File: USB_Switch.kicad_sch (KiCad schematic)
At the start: 2 parts, among them J1 Conn_01x06, J4 Conn_01x08

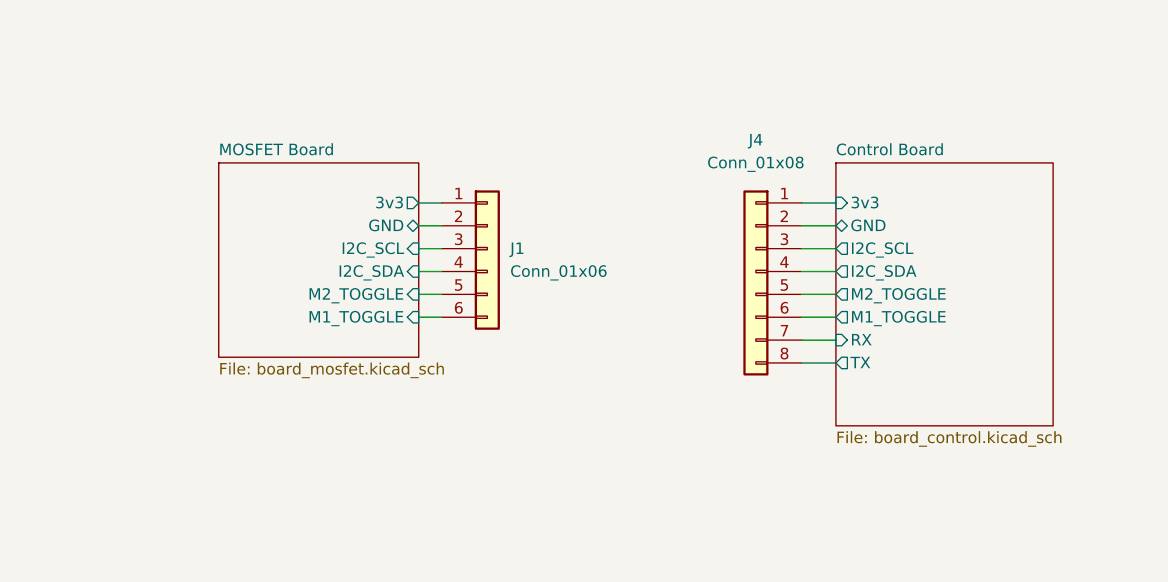
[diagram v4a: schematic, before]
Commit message: Made schematics pretty, added photos, added README
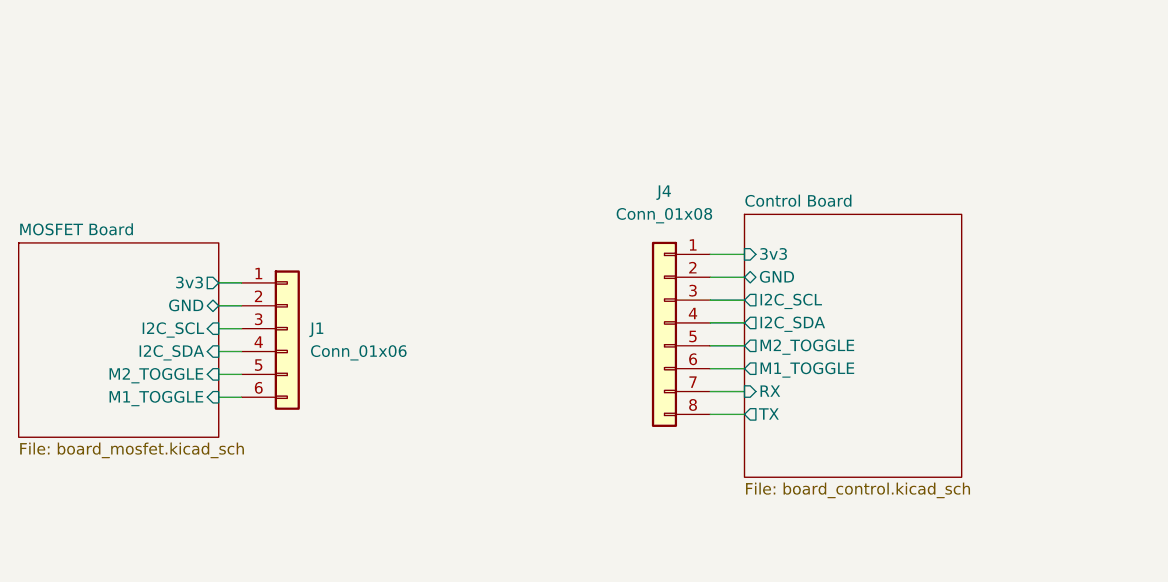
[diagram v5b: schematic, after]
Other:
- title: Smart USB Port -> Wifi USB Port
- moved on the sheet: J1, J4
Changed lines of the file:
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@@
 (kicad_sch (version 20211123) (generator eeschema)
-  (paper "A4")
+  (paper "A5")
   (title_block
-    (title "Smart USB Port")
-    (date "2022-10-23")
-    (rev "0.1")
+    (title "Wifi USB Port")
+    (date "2023-02-05")
+    (rev "0.2.0")
   )
-  (wire (pts (xy 137.795 48.895) (xy 141.605 48.895))
+  (wire (pts (xy 127.635 54.61) (xy 131.445 54.61))
     (stroke (width 0) (type default) (color 0 0 0 0))
   )
-  (wire (pts (xy 137.795 51.435) (xy 141.605 51.435))
+  (wire (pts (xy 127.635 57.15) (xy 131.445 57.15))
     (stroke (width 0) (type default) (color 0 0 0 0))
   )
-  (wire (pts (xy 137.795 59.055) (xy 141.605 59.055))
+  (wire (pts (xy 127.635 64.77) (xy 131.445 64.77))
     (stroke (width 0) (type default) (color 0 0 0 0))
   )
-  (wire (pts (xy 137.795 53.975) (xy 141.605 53.975))
+  (wire (pts (xy 127.635 59.69) (xy 131.445 59.69))
     (stroke (width 0) (type default) (color 0 0 0 0))
   )
-  (wire (pts (xy 97.79 61.595) (xy 95.25 61.595))
+  (wire (pts (xy 75.565 70.485) (xy 73.025 70.485))
     (stroke (width 0) (type default) (color 0 0 0 0))
   )
-  (wire (pts (xy 137.795 64.135) (xy 141.605 64.135))
+  (wire (pts (xy 127.635 69.85) (xy 131.445 69.85))
     (stroke (width 0) (type default) (color 0 0 0 0))
   )
-  (wire (pts (xy 97.79 59.055) (xy 95.25 59.055))
+  (wire (pts (xy 75.565 67.945) (xy 73.025 67.945))
     (stroke (width 0) (type default) (color 0 0 0 0))
   )
-  (wire (pts (xy 97.79 56.515) (xy 95.25 56.515))
+  (wire (pts (xy 75.565 65.405) (xy 73.025 65.405))
     (stroke (width 0) (type default) (color 0 0 0 0))
   )
-  (wire (pts (xy 137.795 61.595) (xy 141.605 61.595))
+  (wire (pts (xy 127.635 67.31) (xy 131.445 67.31))
     (stroke (width 0) (type default) (color 0 0 0 0))
   )
-  (wire (pts (xy 97.79 51.435) (xy 95.25 51.435))
+  (wire (pts (xy 75.565 60.325) (xy 73.025 60.325))
     (stroke (width 0) (type default) (color 0 0 0 0))
   )
-  (wire (pts (xy 97.79 48.895) (xy 95.25 48.895))
+  (wire (pts (xy 75.565 57.785) (xy 73.025 57.785))
     (stroke (width 0) (type default) (color 0 0 0 0))
   )
-  (wire (pts (xy 97.79 53.975) (xy 95.25 53.975))
+  (wire (pts (xy 75.565 62.865) (xy 73.025 62.865))
     (stroke (width 0) (type default) (color 0 0 0 0))
   )
-  (wire (pts (xy 137.795 66.675) (xy 141.605 66.675))
+  (wire (pts (xy 127.635 72.39) (xy 131.445 72.39))
     (stroke (width 0) (type default) (color 0 0 0 0))
   )
-  (wire (pts (xy 137.795 56.515) (xy 141.605 56.515))
+  (wire (pts (xy 127.635 62.23) (xy 131.445 62.23))
     (stroke (width 0) (type default) (color 0 0 0 0))
   )
-  (symbol (lib_id "Connector_Generic:Conn_01x08") (at 132.715 56.515 0) (mirror y) (unit 1)
+  (symbol (lib_id "Connector_Generic:Conn_01x08") (at 122.555 62.23 0) (mirror y) (unit 1)
     (in_bom yes) (on_board yes) (fields_autoplaced)
-    (property "Reference" "J4" (id 0) (at 132.715 41.91 0))
-    (property "Value" "Conn_01x08" (id 1) (at 132.715 44.45 0))
-    (property "Footprint" "Connector_PinHeader_2.54mm:PinHeader_1x08_P2.54mm_Vertical" (id 2) (at 132.715 56.515 0)
+    (property "Reference" "J4" (id 0) (at 122.555 47.625 0))
+    (property "Value" "Conn_01x08" (id 1) (at 122.555 50.165 0))
+    (property "Footprint" "Connector_PinHeader_2.54mm:PinHeader_1x08_P2.54mm_Vertical" (id 2) (at 122.555 62.23 0)
       (effects (font (size 1.27 1.27)) hide)
     )
-    (property "Datasheet" "~" (id 3) (at 132.715 56.515 0)
+    (property "Datasheet" "~" (id 3) (at 122.555 62.23 0)
       (effects (font (size 1.27 1.27)) hide)
     )
@@
     (pin "8")
   )
-  (symbol (lib_id "Connector_Generic:Conn_01x06") (at 102.87 53.975 0) (unit 1)
+  (symbol (lib_id "Connector_Generic:Conn_01x06") (at 80.645 62.865 0) (unit 1)
     (in_bom yes) (on_board yes) (fields_autoplaced)
-    (property "Reference" "J1" (id 0) (at 105.41 53.9749 0)
+    (property "Reference" "J1" (id 0) (at 83.185 62.8649 0)
       (effects (font (size 1.27 1.27)) (justify left))
     )
-    (property "Value" "Conn_01x06" (id 1) (at 105.41 56.5149 0)
+    (property "Value" "Conn_01x06" (id 1) (at 83.185 65.4049 0)
       (effects (font (size 1.27 1.27)) (justify left))
     )
-    (property "Footprint" "Connector_PinHeader_2.54mm:PinHeader_1x06_P2.54mm_Vertical" (id 2) (at 102.87 53.975 0)
+    (property "Footprint" "Connector_PinHeader_2.54mm:PinHeader_1x06_P2.54mm_Vertical" (id 2) (at 80.645 62.865 0)
       (effects (font (size 1.27 1.27)) hide)
     )
-    (property "Datasheet" "~" (id 3) (at 102.87 53.975 0)
+    (property "Datasheet" "~" (id 3) (at 80.645 62.865 0)
       (effects (font (size 1.27 1.27)) hide)
     )
-    (property "LCSC Part Number" "" (id 4) (at 102.87 53.975 0)
+    (property "LCSC Part Number" "" (id 4) (at 80.645 62.865 0)
       (effects (font (size 1.27 1.27)) hide)
     )
-    (property "Manufacturer" "" (id 5) (at 102.87 53.975 0)
+    (property "Manufacturer" "" (id 5) (at 80.645 62.865 0)
       (effects (font (size 1.27 1.27)) hide)
     )
-    (property "Manufacturer Part Number" "" (id 6) (at 102.87 53.975 0)
+    (property "Manufacturer Part Number" "" (id 6) (at 80.645 62.865 0)
       (effects (font (size 1.27 1.27)) hide)
     )
@@
     (pin "6")
   )
-  (sheet (at 141.605 44.45) (size 24.13 29.21) (fields_autoplaced)
+  (sheet (at 131.445 50.165) (size 24.13 29.21) (fields_autoplaced)
     (stroke (width 0.1524) (type solid) (color 0 0 0 0))
     (fill (color 0 0 0 0.0000))
-    (property "Sheet name" "Control Board" (id 0) (at 141.605 43.7384 0)
+    (property "Sheet name" "Control Board" (id 0) (at 131.445 49.4534 0)
       (effects (font (size 1.27 1.27)) (justify left bottom))
     )
-    (property "Sheet file" "board_control.kicad_sch" (id 1) (at 141.605 74.2446 0)
+    (property "Sheet file" "board_control.kicad_sch" (id 1) (at 131.445 79.9596 0)
       (effects (font (size 1.27 1.27)) (justify left top))
     )
-    (pin "3v3" input (at 141.605 48.895 180)
+    (pin "3v3" input (at 131.445 54.61 180)
       (effects (font (size 1.27 1.27)) (justify left))
     )
-    (pin "GND" bidirectional (at 141.605 51.435 180)
+    (pin "GND" bidirectional (at 131.445 57.15 180)
       (effects (font (size 1.27 1.27)) (justify left))
     )
-    (pin "I2C_SCL" output (at 141.605 53.975 180)
+    (pin "I2C_SCL" output (at 131.445 59.69 180)
       (effects (font (size 1.27 1.27)) (justify left))
     )
-    (pin "I2C_SDA" output (at 141.605 56.515 180)
+    (pin "I2C_SDA" output (at 131.445 62.23 180)
       (effects (font (size 1.27 1.27)) (justify left))
     )
-    (pin "M2_TOGGLE" output (at 141.605 59.055 180)
+    (pin "M2_TOGGLE" output (at 131.445 64.77 180)
       (effects (font (size 1.27 1.27)) (justify left))
     )
-    (pin "M1_TOGGLE" output (at 141.605 61.595 180)
+    (pin "M1_TOGGLE" output (at 131.445 67.31 180)
       (effects (font (size 1.27 1.27)) (justify left))
     )
-    (pin "TX" output (at 141.605 66.675 180)
+    (pin "TX" output (at 131.445 72.39 180)
       (effects (font (size 1.27 1.27)) (justify left))
     )
-    (pin "RX" input (at 141.605 64.135 180)
+    (pin "RX" input (at 131.445 69.85 180)
       (effects (font (size 1.27 1.27)) (justify left))
     )
   )
-  (sheet (at 73.025 44.45) (size 22.225 21.59) (fields_autoplaced)
+  (sheet (at 50.8 53.34) (size 22.225 21.59) (fields_autoplaced)
     (stroke (width 0.1524) (type solid) (color 0 0 0 0))
     (fill (color 0 0 0 0.0000))
-    (property "Sheet name" "MOSFET Board" (id 0) (at 73.025 43.7384 0)
+    (property "Sheet name" "MOSFET Board" (id 0) (at 50.8 52.6284 0)
       (effects (font (size 1.27 1.27)) (justify left bottom))
     )
-    (property "Sheet file" "board_mosfet.kicad_sch" (id 1) (at 73.025 66.6246 0)
+    (property "Sheet file" "board_mosfet.kicad_sch" (id 1) (at 50.8 75.5146 0)
       (effects (font (size 1.27 1.27)) (justify left top))
     )
-    (pin "3v3" output (at 95.25 48.895 0)
+    (pin "3v3" output (at 73.025 57.785 0)
       (effects (font (size 1.27 1.27)) (justify right))
     )
-    (pin "GND" bidirectional (at 95.25 51.435 0)
+    (pin "GND" bidirectional (at 73.025 60.325 0)
       (effects (font (size 1.27 1.27)) (justify right))
     )
-    (pin "I2C_SCL" input (at 95.25 53.975 0)
+    (pin "I2C_SCL" input (at 73.025 62.865 0)
       (effects (font (size 1.27 1.27)) (justify right))
     )
-    (pin "I2C_SDA" input (at 95.25 56.515 0)
+    (pin "I2C_SDA" input (at 73.025 65.405 0)
       (effects (font (size 1.27 1.27)) (justify right))
     )
-    (pin "M2_TOGGLE" input (at 95.25 59.055 0)
+    (pin "M2_TOGGLE" input (at 73.025 67.945 0)
       (effects (font (size 1.27 1.27)) (justify right))
     )
-    (pin "M1_TOGGLE" input (at 95.25 61.595 0)
+    (pin "M1_TOGGLE" input (at 73.025 70.485 0)
       (effects (font (size 1.27 1.27)) (justify right))
     )

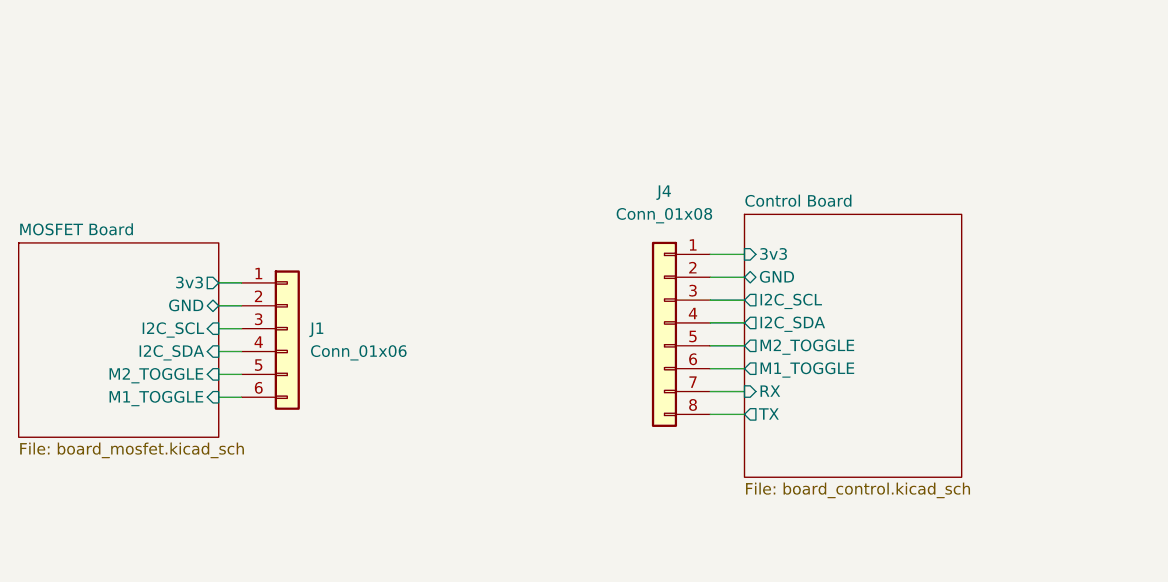
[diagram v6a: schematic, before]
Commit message: Initial change moving items to back of PCB
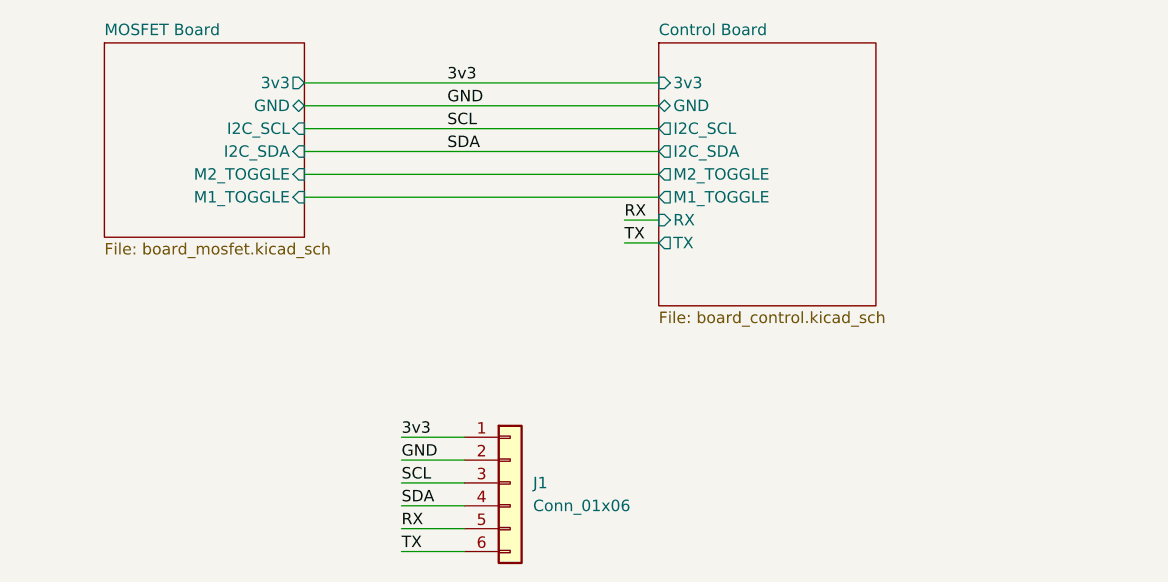
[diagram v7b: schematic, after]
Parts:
- removed J4: Conn_01x08, Connector_PinHeader_2.54mm:PinHeader_1x08_P2.54mm_Vertical, symbol Connector_Generic:Conn_01x08
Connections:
- net MOSFET Board/3v3 renamed 3v3
- net MOSFET Board/GND renamed GND
- net MOSFET Board/I2C_SCL renamed SCL
- net MOSFET Board/I2C_SDA renamed SDA
- net MOSFET Board/M1_TOGGLE renamed TX
- net MOSFET Board/M2_TOGGLE renamed RX
